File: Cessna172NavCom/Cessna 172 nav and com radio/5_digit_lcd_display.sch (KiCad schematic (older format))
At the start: 7 parts, among them U1 MAX7219 COM standby

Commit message: Add rotary encoder
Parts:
- LED1, LED2, LED3, LED4, LED5: footprint Display_7Segment:KCSC02-105 -> Cessna 172 nav and com radio:KYX-5101AS
- U1: footprint Package_DIP:DIP-24_W7.62mm -> Package_SO:SSOP-24_3.9x8.7mm_P0.635mm
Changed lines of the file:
@@
 F 0 "U1" H 2500 5000 50  0000 C CNN
 F 1 "MAX7219 COM standby" V 2350 4100 50  0000 C CNN
-F 2 "Package_DIP:DIP-24_W7.62mm" H 2700 4100 50  0001 C CNN
+F 2 "Package_SO:SSOP-24_3.9x8.7mm_P0.635mm" H 2700 4100 50  0001 C CNN
 F 3 "https://datasheets.maximintegrated.com/en/ds/MAX7219-MAX7221.pdf" H 2800 3900 50  0001 C CNN
 	1    2750 4050
@@
 F 0 "LED1" H 4350 2900 50  0000 C CNN
 F 1 "MobiFlight digit 5" H 4350 3000 50  0000 C CNN
-F 2 "Display_7Segment:KCSC02-105" H 4350 2950 50  0001 C CNN
+F 2 "Cessna 172 nav and com radio:KYX-5101AS" H 4350 2950 50  0001 C CNN
 F 3 "http://www.kingbright.com/attachments/file/psearch/000/00/00/KCSC02-105(Ver.9A).pdf" H 3850 4025 50  0001 L CNN
 	1    4350 3550
@@
 F 0 "LED2" H 5600 2900 50  0000 C CNN
 F 1 "MobiFlight digit 4" H 5600 3000 50  0000 C CNN
-F 2 "Display_7Segment:KCSC02-105" H 5600 2950 50  0001 C CNN
+F 2 "Cessna 172 nav and com radio:KYX-5101AS" H 5600 2950 50  0001 C CNN
 F 3 "http://www.kingbright.com/attachments/file/psearch/000/00/00/KCSC02-105(Ver.9A).pdf" H 5100 4025 50  0001 L CNN
 	1    5600 3550
@@
 F 0 "LED3" H 6850 2900 50  0000 C CNN
 F 1 "MobiFlight digit 2" H 6850 3000 50  0000 C CNN
-F 2 "Display_7Segment:KCSC02-105" H 6850 2950 50  0001 C CNN
+F 2 "Cessna 172 nav and com radio:KYX-5101AS" H 6850 2950 50  0001 C CNN
 F 3 "http://www.kingbright.com/attachments/file/psearch/000/00/00/KCSC02-105(Ver.9A).pdf" H 6350 4025 50  0001 L CNN
 	1    6850 3550
@@
 F 0 "LED4" H 8100 2900 50  0000 C CNN
 F 1 "MobiFlight digit 1" H 8100 3000 50  0000 C CNN
-F 2 "Display_7Segment:KCSC02-105" H 8100 2950 50  0001 C CNN
+F 2 "Cessna 172 nav and com radio:KYX-5101AS" H 8100 2950 50  0001 C CNN
 F 3 "http://www.kingbright.com/attachments/file/psearch/000/00/00/KCSC02-105(Ver.9A).pdf" H 7600 4025 50  0001 L CNN
 	1    8100 3550
@@
 F 0 "LED5" H 9350 2900 50  0000 C CNN
 F 1 "Mobiflight digit 0" H 9350 3000 50  0000 C CNN
-F 2 "Display_7Segment:KCSC02-105" H 9350 2950 50  0001 C CNN
+F 2 "Cessna 172 nav and com radio:KYX-5101AS" H 9350 2950 50  0001 C CNN
 F 3 "http://www.kingbright.com/attachments/file/psearch/000/00/00/KCSC02-105(Ver.9A).pdf" H 8850 4025 50  0001 L CNN
 	1    9350 3550

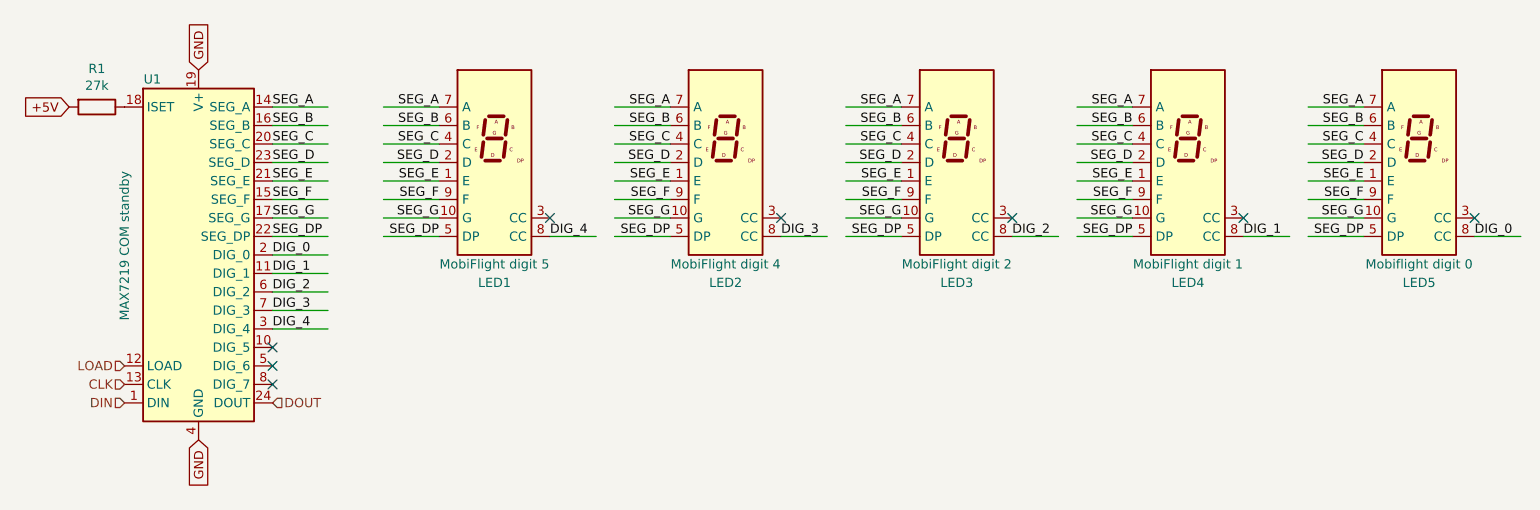
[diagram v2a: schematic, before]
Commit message: Proper LED buttons and switches
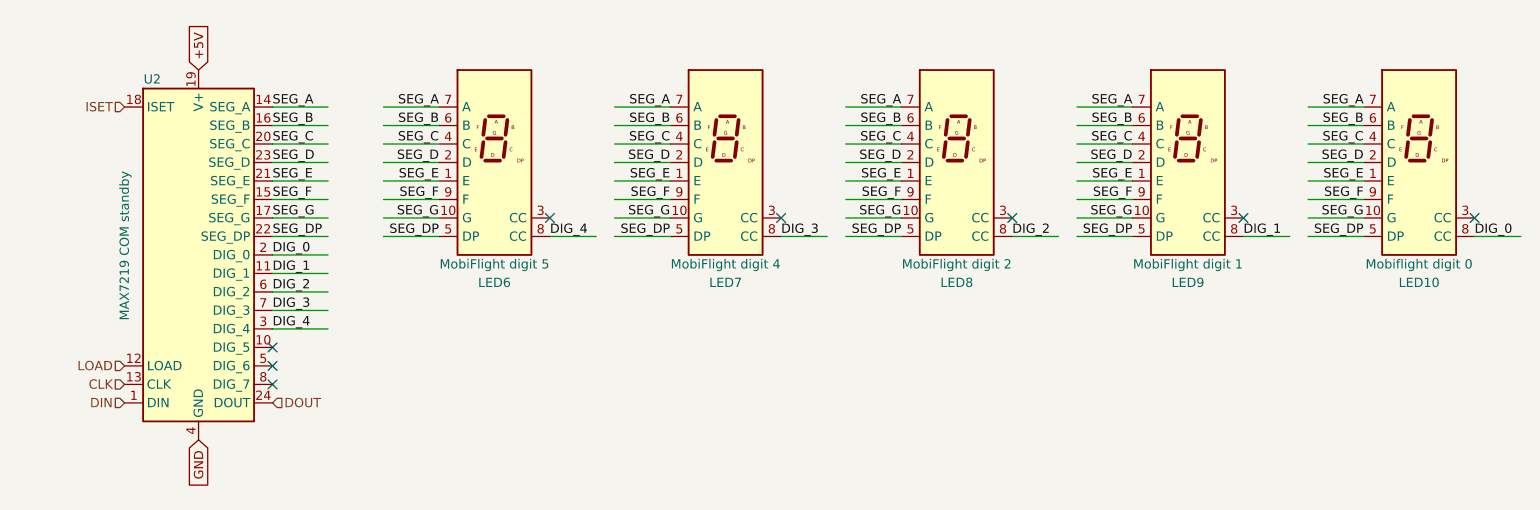
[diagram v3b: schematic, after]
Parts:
- removed R1: 27k, Resistor_SMD:R_0805_2012Metric_Pad1.15x1.40mm_HandSolder, symbol Device:R
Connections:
- net labels added: ISET
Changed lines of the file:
@@
 $Descr A4 11693 8268
 encoding utf-8
-Sheet 2 7
+Sheet 3 8
 Title ""
 Date ""
@@
 AR Path="/5F613967/5F60E2D2" Ref="U3"  Part="1"
 AR Path="/5F613974/5F60E2D2" Ref="U4"  Part="1"
-F 0 "U1" H 2500 5000 50  0000 C CNN
+F 0 "U2" H 2500 5000 50  0000 C CNN
 F 1 "MAX7219 COM standby" V 2350 4100 50  0000 C CNN
 F 2 "Package_SO:SSOP-24_3.9x8.7mm_P0.635mm" H 2700 4100 50  0001 C CNN
@@
 	1    2750 4050
 	1    0    0    -1
-$EndComp
-$Comp
-L Device:R R?
-U 1 1 5F60E2D8
-P 2200 3250
-AR Path="/5F60E2D8" Ref="R?"  Part="1"
-AR Path="/5F60A880/5F60E2D8" Ref="R1"  Part="1"
-AR Path="/5F61163D/5F60E2D8" Ref="R2"  Part="1"
-AR Path="/5F613967/5F60E2D8" Ref="R3"  Part="1"
-AR Path="/5F613974/5F60E2D8" Ref="R4"  Part="1"
-F 0 "R1" V 1993 3250 50  0000 C CNN
-F 1 "27k" V 2084 3250 50  0000 C CNN
-F 2 "Resistor_SMD:R_0805_2012Metric_Pad1.15x1.40mm_HandSolder" V 2130 3250 50  0001 C CNN
-F 3 "~" H 2200 3250 50  0001 C CNN
-	1    2200 3250
-	0    1    1    0
 $EndComp
 $Comp
@@
 AR Path="/5F613967/5F60E2DE" Ref="LED11"  Part="1"
 AR Path="/5F613974/5F60E2DE" Ref="LED16"  Part="1"
-F 0 "LED1" H 4350 2900 50  0000 C CNN
+F 0 "LED6" H 4350 2900 50  0000 C CNN
 F 1 "MobiFlight digit 5" H 4350 3000 50  0000 C CNN
 F 2 "Cessna 172 nav and com radio:KYX-5101AS" H 4350 2950 50  0001 C CNN
@@
 NoConn ~ 3150 4650
 NoConn ~ 3150 4750
-Text GLabel 2050 3250 0    50   Input ~ 0
+Text GLabel 2750 3050 1    50   Input ~ 0
 +5V
-Text GLabel 2750 3050 1    50   Input ~ 0
-GND
 Text GLabel 2750 5050 3    50   Input ~ 0
 GND
@@
 AR Path="/5F613967/5F60E317" Ref="LED12"  Part="1"
 AR Path="/5F613974/5F60E317" Ref="LED17"  Part="1"
-F 0 "LED2" H 5600 2900 50  0000 C CNN
+F 0 "LED7" H 5600 2900 50  0000 C CNN
 F 1 "MobiFlight digit 4" H 5600 3000 50  0000 C CNN
 F 2 "Cessna 172 nav and com radio:KYX-5101AS" H 5600 2950 50  0001 C CNN
@@
 AR Path="/5F613967/5F60E330" Ref="LED13"  Part="1"
 AR Path="/5F613974/5F60E330" Ref="LED18"  Part="1"
-F 0 "LED3" H 6850 2900 50  0000 C CNN
+F 0 "LED8" H 6850 2900 50  0000 C CNN
 F 1 "MobiFlight digit 2" H 6850 3000 50  0000 C CNN
 F 2 "Cessna 172 nav and com radio:KYX-5101AS" H 6850 2950 50  0001 C CNN
@@
 AR Path="/5F613967/5F60E349" Ref="LED14"  Part="1"
 AR Path="/5F613974/5F60E349" Ref="LED19"  Part="1"
-F 0 "LED4" H 8100 2900 50  0000 C CNN
+F 0 "LED9" H 8100 2900 50  0000 C CNN
 F 1 "MobiFlight digit 1" H 8100 3000 50  0000 C CNN
 F 2 "Cessna 172 nav and com radio:KYX-5101AS" H 8100 2950 50  0001 C CNN
@@
 AR Path="/5F613967/5F60E362" Ref="LED15"  Part="1"
 AR Path="/5F613974/5F60E362" Ref="LED20"  Part="1"
-F 0 "LED5" H 9350 2900 50  0000 C CNN
+F 0 "LED10" H 9350 2900 50  0000 C CNN
 F 1 "Mobiflight digit 0" H 9350 3000 50  0000 C CNN
 F 2 "Cessna 172 nav and com radio:KYX-5101AS" H 9350 2950 50  0001 C CNN
@@
 Text HLabel 2350 4850 0    50   Input ~ 0
 DIN
+Text HLabel 2350 3250 0    50   Input ~ 0
+ISET
 $EndSCHEMATC
